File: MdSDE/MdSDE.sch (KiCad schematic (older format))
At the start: 0 parts

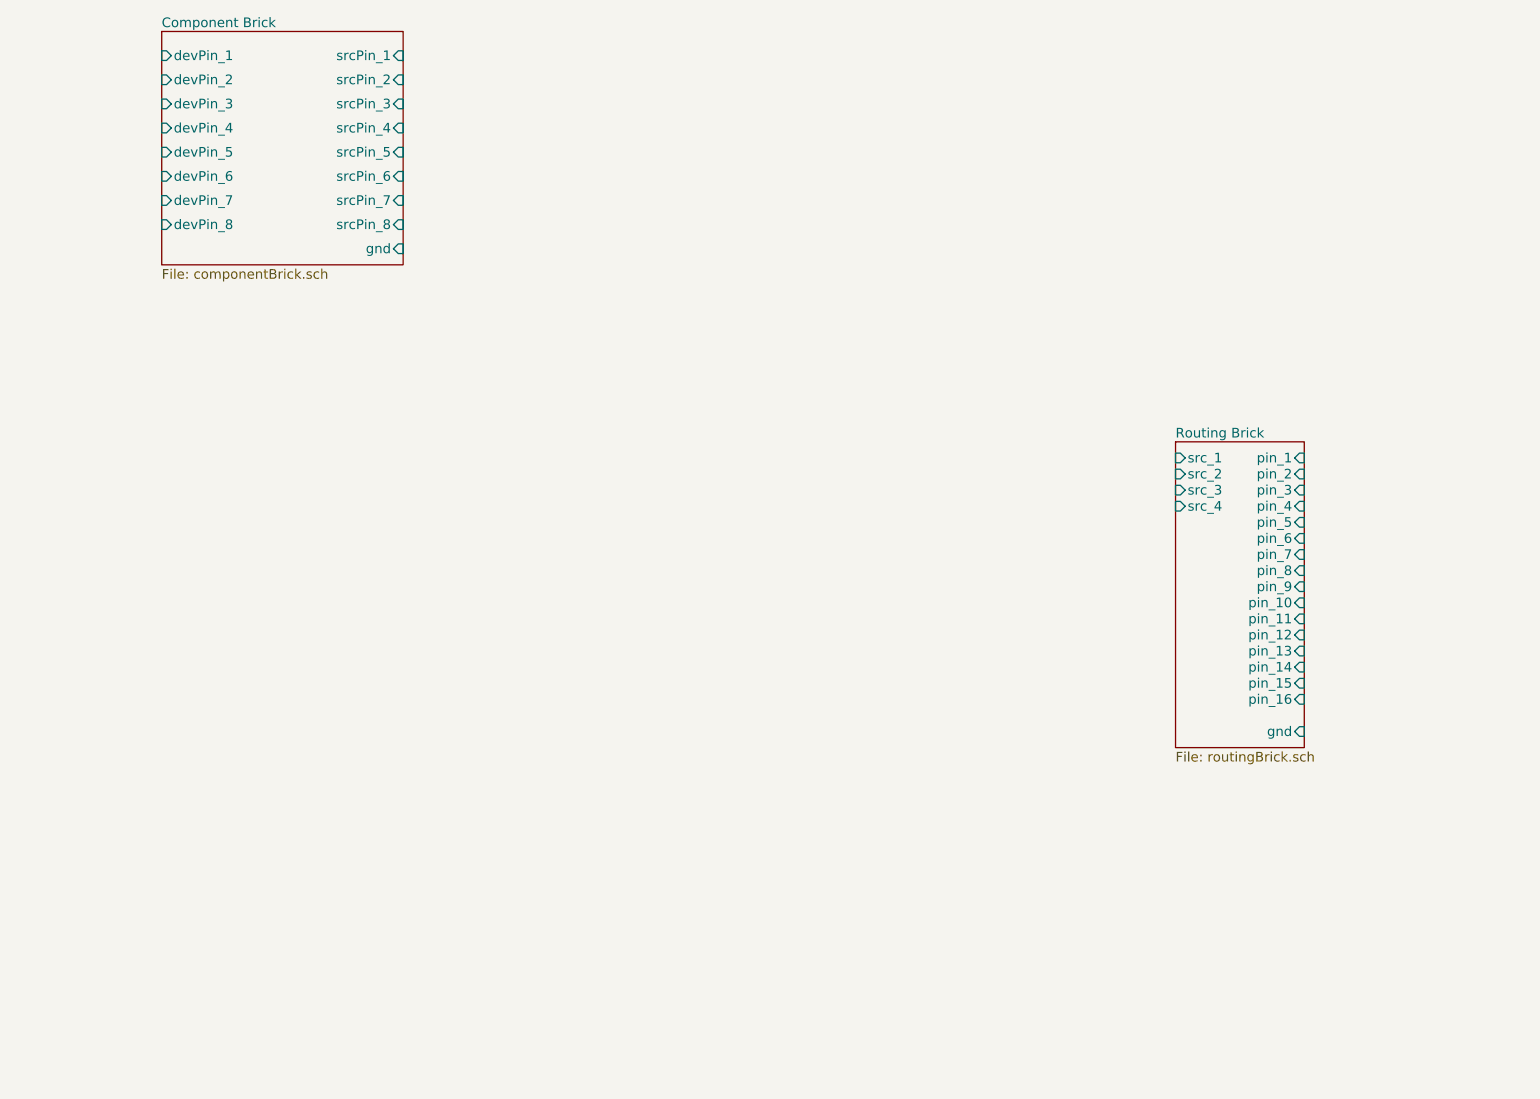
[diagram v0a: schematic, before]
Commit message: Finished board schematic
Completed schematic for test board
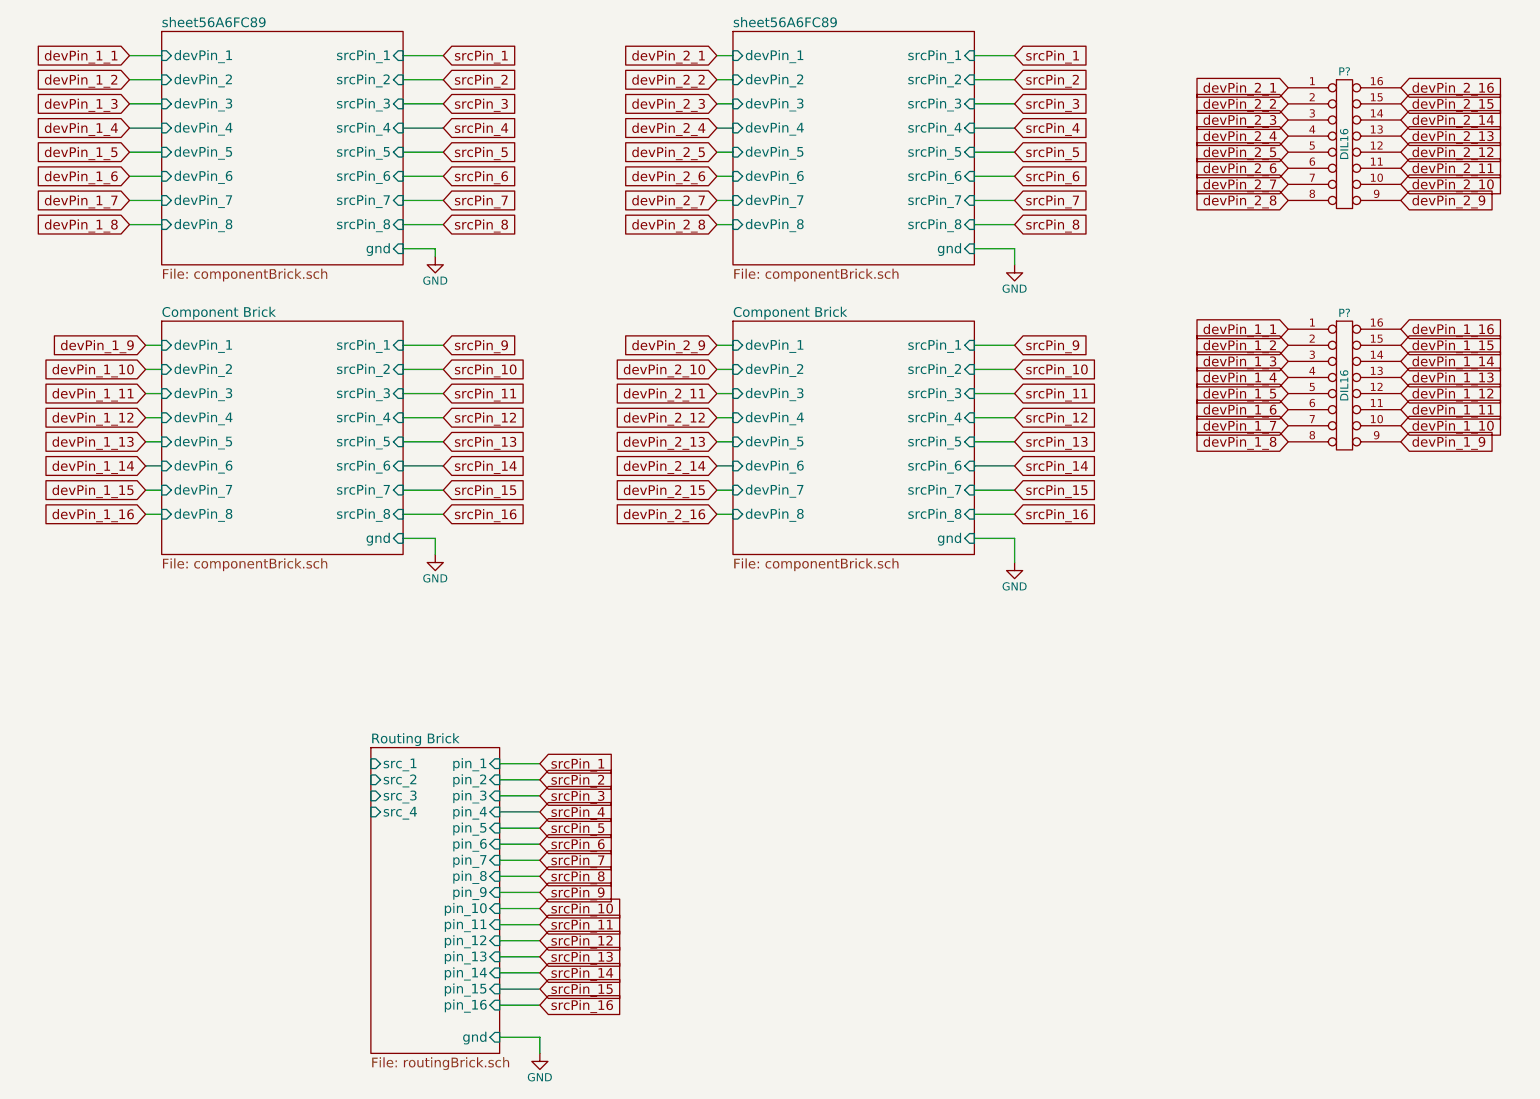
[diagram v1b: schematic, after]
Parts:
- added P? (x2): DIL16, symbol DIL16
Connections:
- new net devPin_1_1: P?.1
- new net devPin_1_10: P?.10
- new net devPin_1_11: P?.11
- new net devPin_1_12: P?.12
- new net devPin_1_13: P?.13
- new net devPin_1_14: P?.14
- new net devPin_1_15: P?.15
- new net devPin_1_16: P?.16
- new net devPin_1_2: P?.2
- new net devPin_1_3: P?.3
- new net devPin_1_4: P?.4
- new net devPin_1_5: P?.5
- new net devPin_1_6: P?.6
- new net devPin_1_7: P?.7
- new net devPin_1_8: P?.8
- new net devPin_1_9: P?.9
- new net devPin_2_1: P?.1
- new net devPin_2_10: P?.10
- new net devPin_2_11: P?.11
- new net devPin_2_12: P?.12
- new net devPin_2_13: P?.13
- new net devPin_2_14: P?.14
- new net devPin_2_15: P?.15
- new net devPin_2_16: P?.16
- new net devPin_2_2: P?.2
- new net devPin_2_3: P?.3
- new net devPin_2_4: P?.4
- new net devPin_2_5: P?.5
- new net devPin_2_6: P?.6
- new net devPin_2_7: P?.7
- new net devPin_2_8: P?.8
- new net devPin_2_9: P?.9
